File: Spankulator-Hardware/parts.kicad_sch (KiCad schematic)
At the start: 41 parts, among them J11 OLED Pins, J14 Eurorack Power Cable, M2 OLED

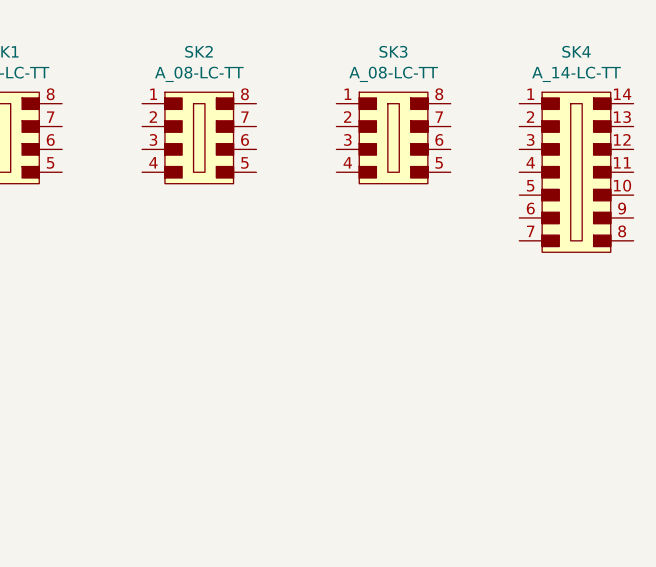
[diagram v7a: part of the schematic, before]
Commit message: Adds socket for OP Amp
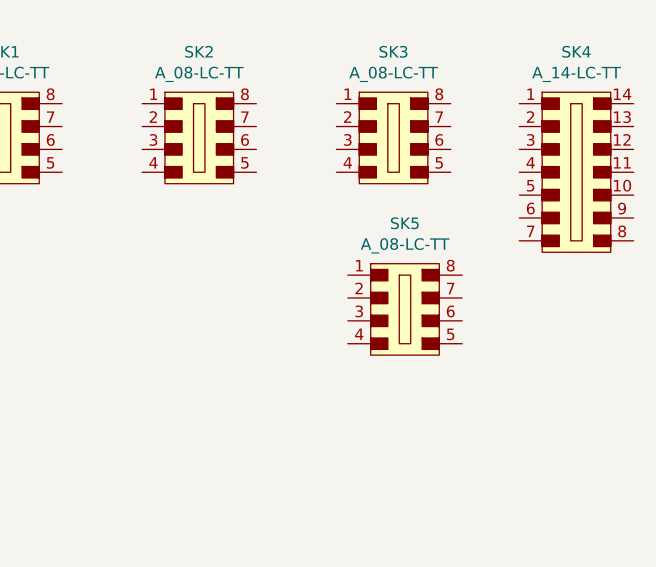
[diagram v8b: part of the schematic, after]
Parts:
- added SK5: A_08-LC-TT, Package_DIP:DIP-8_W7.62mm_Socket, symbol dk_Sockets-for-ICs-Transistors:A_08-LC-TT
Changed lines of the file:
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@@
     )
+  )
+  (symbol (lib_id "dk_Sockets-for-ICs-Transistors:A_08-LC-TT") (at 206.375 67.31 0) (unit 1)
+    (in_bom yes) (on_board no)
+    (property "Reference" "SK5" (id 0) (at 206.375 57.785 0))
+    (property "Value" "A_08-LC-TT" (id 1) (at 206.375 60.0964 0))
+    (property "Footprint" "Package_DIP:DIP-8_W7.62mm_Socket" (id 2) (at 211.455 62.23 0)
+      (effects (font (size 1.524 1.524)) (justify left) hide)
+    )
+    (property "Datasheet" "http://www.assmann-wsw.com/fileadmin/datasheets/ASS_0810_CO.pdf" (id 3) (at 211.455 59.69 0)
+      (effects (font (size 1.524 1.524)) (justify left) hide)
+    )
+    (property "Digi-Key Part" "AE9986-ND" (id 4) (at 211.455 57.15 0)
+      (effects (font (size 1.524 1.524)) (justify left) hide)
+    )
+    (property "LCSC Part #" "none" (id 5) (at 206.375 67.31 0)
+      (effects (font (size 1.27 1.27)) hide)
+    )
+    (property "Build Type" "" (id 6) (at 206.375 67.31 0)
+      (effects (font (size 1.27 1.27)) hide)
+    )
+    (pin "1")
+    (pin "2")
+    (pin "3")
+    (pin "4")
+    (pin "5")
+    (pin "6")
+    (pin "7")
+    (pin "8")
   )
   (symbol (lib_id "Mechanical:MountingHole") (at 61.595 55.88 0) (unit 1)
